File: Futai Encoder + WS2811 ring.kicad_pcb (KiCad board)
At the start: 2 copper layers, 32 x 49 mm, 41 parts, among them J1 Conn_02x05_Top_Bottom, SW1 RotaryEncoder_Switch_RGB

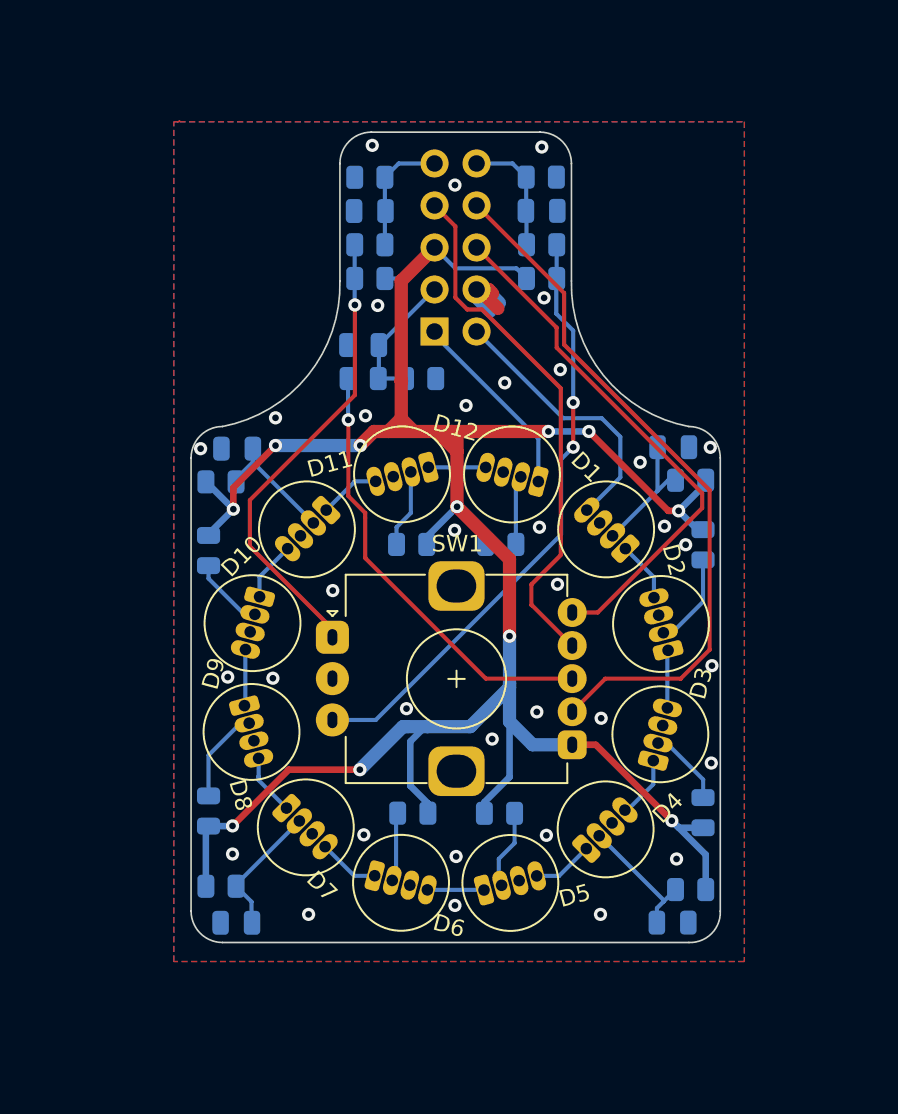
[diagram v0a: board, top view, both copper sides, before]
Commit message: smaller board width, new component placements and better track routing
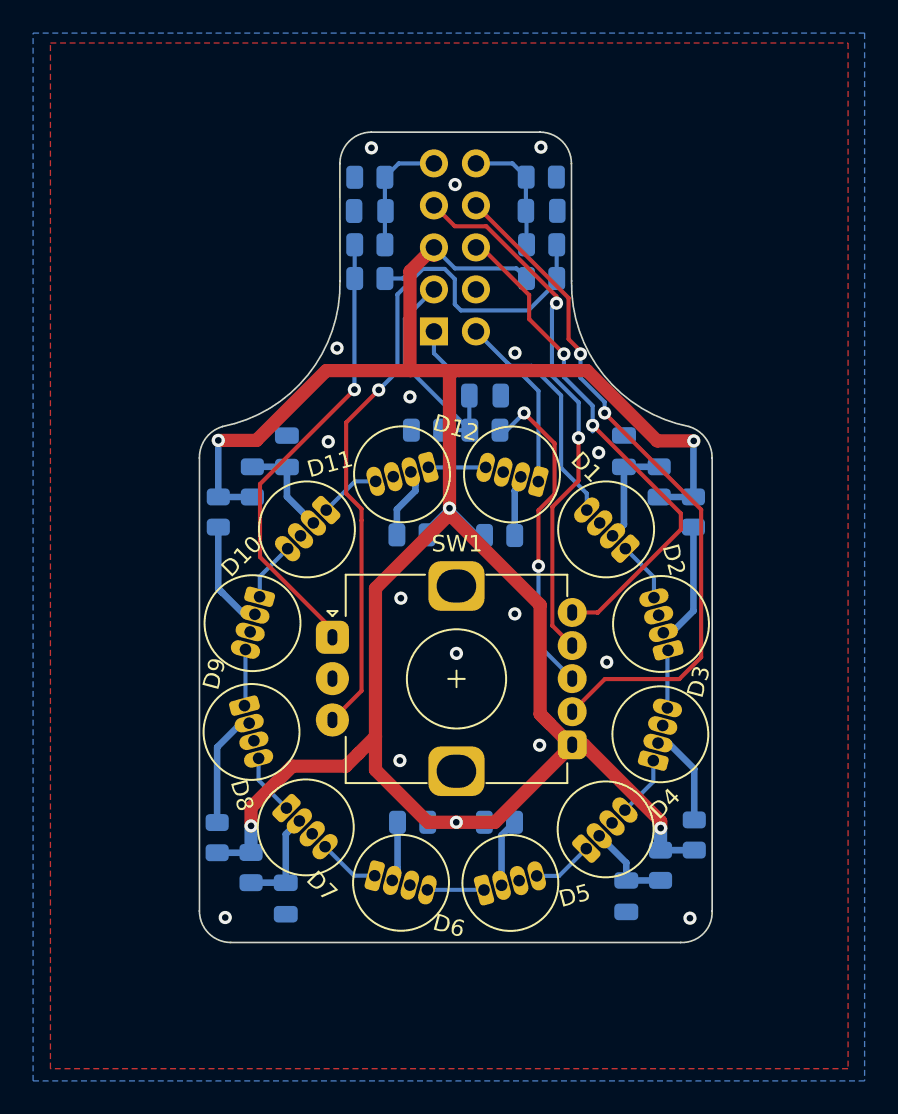
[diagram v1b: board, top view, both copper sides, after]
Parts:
- R1, R10, R11, R12, R2, R3, R4, R5, R6, R7, R8, R9: value 160 -> 130
- moved R21 7.99 mm to (150.3, 84.1), turned to 0 degrees
- moved C21 7.98 mm to (150.3, 82.0), turned to 0 degrees
- moved C7 3.33 mm to (138.2, 112.4), turned to -90 degrees
- moved C4 3.22 mm to (158.8, 112.3), turned to 90 degrees
- moved R22 3.14 mm to (146.7, 84.1), turned to 0 degrees
- moved C10 3.01 mm to (138.3, 85.4), turned to 90 degrees
- moved C1 2.99 mm to (158.7, 85.4), turned to 90 degrees
- moved R9 2.40 mm to (134.1, 89.1)
- moved R4 2.34 mm to (160.9, 110.4), turned to -90 degrees
- moved R7 2.14 mm to (136.1, 110.6), turned to -90 degrees
- moved R2 2.06 mm to (162.9, 89.1)
- moved R1 1.90 mm to (160.8, 87.2), turned to 90 degrees
- moved R10 1.90 mm to (136.2, 87.2), turned to 90 degrees
- moved R8 1.69 mm to (134.1, 108.8)
- moved R3 1.45 mm to (162.9, 108.6)
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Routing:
- net GND: track 10.2 -> 3.29 mm, vias 35 -> 16
- net SWC: track 26.8 -> 20.0 mm, vias 1 -> 2
- net ENC_B: track 36.7 -> 43.4 mm, vias 2 -> 1
- net +5V: track 148.1 -> 154.5 mm, vias 11 -> 6
- net Net-(C21-Pad1): track 8.45 -> 14.7 mm
- net Net-(D9-Pad2): track 4.47 -> 7.63 mm
- net Net-(D2-Pad2): track 6.24 -> 9.17 mm
- net Net-(C4-Pad2): track 8.10 -> 5.49 mm
- net DOUT: track 12.0 -> 14.6 mm
- net Net-(D8-Pad2): track 6.17 -> 8.51 mm
- net Net-(D3-Pad2): track 5.30 -> 7.47 mm
- net DIN: track 16.6 -> 14.6 mm
- net Net-(C7-Pad1): track 8.16 -> 6.27 mm
- net Net-(C10-Pad1): track 7.63 -> 6.16 mm
- net Net-(D12-Pad2): track 4.21 -> 5.47 mm
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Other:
- board size 32 x 49 mm -> 31 x 49 mm
- board text added: "5V"
- board text added: "BLU"
- board text added: "Din"
- board text added: "Dout"
- board text added: "EncB"
- board text added: "GND"
- board text added: "GRE"
- board text added: "RED"
- board text added: "SWC"
- board text added: "https://github.com/andilge"
- board text added: "v0.65"
- board text removed: "A|GR|5|SW|DO"
- board text removed: "B|BL|RE|G|DI"
- board text removed: "https//github.com/andilge"
- board text removed: "v0.5"

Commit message: fixing wrong header pin descrition on borad
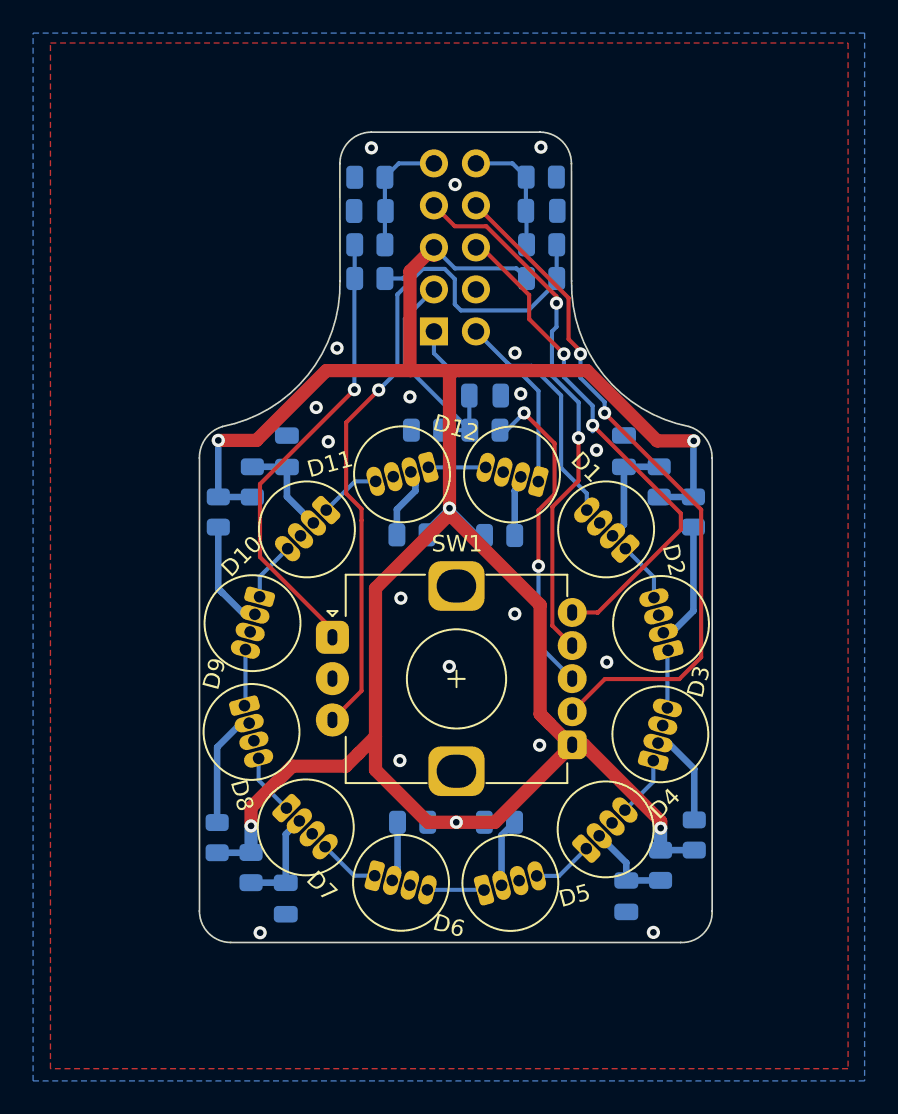
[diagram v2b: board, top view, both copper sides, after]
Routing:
- net GND: vias 16 -> 18
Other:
- board text added: "EncA"
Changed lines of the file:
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@@
     (effects (font (size 0.65 0.65) (thickness 0.1)) (justify mirror))
   )
-  (gr_text "EncB" (at 145.41 68 270) (layer "B.SilkS")
+  (gr_text "EncA" (at 145.41 68 270) (layer "B.SilkS")
     (effects (font (size 0.65 0.65) (thickness 0.1)) (justify mirror))
   )
@@
   (segment (start 145.721259 111.63235) (end 145.721259 112.178741) (width 0.25) (layer "F.Cu") (net 2))
   (segment (start 136.05765 96.321259) (end 135.521259 96.321259) (width 0.25) (layer "F.Cu") (net 2))
-  (via (at 148.54 97.62) (size 0.8) (drill 0.4) (layers "F.Cu" "B.Cu") (free) (net 2))
-  (via (at 157.14 85.48) (size 0.8) (drill 0.4) (layers "F.Cu" "B.Cu") (free) (net 2))
+  (via (at 148.11 98.41) (size 0.8) (drill 0.4) (layers "F.Cu" "B.Cu") (free) (net 2))
+  (via (at 157.01 85.33) (size 0.8) (drill 0.4) (layers "F.Cu" "B.Cu") (free) (net 2))
   (via (at 157.63 98.15) (size 0.8) (drill 0.4) (layers "F.Cu" "B.Cu") (free) (net 2))
   (via (at 143.4 67.05) (size 0.8) (drill 0.4) (layers "F.Cu" "B.Cu") (free) (net 2))
-  (via (at 134.56 113.59) (size 0.8) (drill 0.4) (layers "F.Cu" "B.Cu") (free) (net 2))
+  (via (at 140.06 82.75) (size 0.8) (drill 0.4) (layers "F.Cu" "B.Cu") (free) (net 2))
+  (via (at 136.67 114.51) (size 0.8) (drill 0.4) (layers "F.Cu" "B.Cu") (free) (net 2))
   (via (at 141.32 79.16) (size 0.8) (drill 0.4) (layers "F.Cu" "B.Cu") (free) (net 2))
-  (via (at 162.66 113.63) (size 0.8) (drill 0.4) (layers "F.Cu" "B.Cu") (free) (net 2))
+  (via (at 160.45 114.49) (size 0.8) (drill 0.4) (layers "F.Cu" "B.Cu") (free) (net 2))
   (via (at 140.79 84.82) (size 0.8) (drill 0.4) (layers "F.Cu" "B.Cu") (free) (net 2))
   (via (at 145.12 104.1) (size 0.8) (drill 0.4) (layers "F.Cu" "B.Cu") (free) (net 2))
@@
   (via (at 145.73 82.11) (size 0.8) (drill 0.4) (layers "F.Cu" "B.Cu") (free) (net 2))
   (via (at 152.07 95.23) (size 0.8) (drill 0.4) (layers "F.Cu" "B.Cu") (free) (net 2))
+  (via (at 152.43 81.92) (size 0.8) (drill 0.4) (layers "F.Cu" "B.Cu") (free) (net 2))
   (via (at 153.65 67.01) (size 0.8) (drill 0.4) (layers "F.Cu" "B.Cu") (free) (net 2))
   (segment (start 139.888909 89.731091) (end 139.881091 89.731091) (width 0.25) (layer "B.Cu") (net 3))
@@
   (via (at 155.92 84.59) (size 0.8) (drill 0.4) (layers "F.Cu" "B.Cu") (net 31))
   (via (at 154.59 76.44) (size 0.8) (drill 0.4) (layers "F.Cu" "B.Cu") (net 31))
-  (segment (start 154.315489 76.714511) (end 154.59 76.44) (width 0.25) (layer "B.Cu") (net 31))
-  (segment (start 154.315489 80.829771) (end 154.315489 76.714511) (width 0.25) (layer "B.Cu") (net 31))
-  (segment (start 155.92 84.59) (end 155.93 84.58) (width 0.25) (layer "B.Cu") (net 31))
-  (segment (start 155.93 84.58) (end 155.93 82.444282) (width 0.25) (layer "B.Cu") (net 31))
-  (segment (start 155.93 82.444282) (end 154.315489 80.829771) (width 0.25) (layer "B.Cu") (net 31))
+  (segment (start 155.93 84.58) (end 155.92 84.59) (width 0.25) (layer "B.Cu") (net 31))
+  (segment (start 154.59 76.44) (end 154.59 77.88) (width 0.25) (layer "B.Cu") (net 31))
+  (segment (start 154.315489 78.154511) (end 154.315489 80.829771) (width 0.25) (layer "B.Cu") (net 31))
+  (segment (start 154.59 77.88) (end 154.315489 78.154511) (width 0.25) (layer "B.Cu") (net 31))
+  (segment (start 154.315489 80.829771) (end 155.93 82.444282) (width 0.25) (layer "B.Cu") (net 31))
+  (segment (start 155.93 82.444282) (end 155.93 84.58) (width 0.25) (layer "B.Cu") (net 31))
   (segment (start 154.475522 84.925522) (end 154.475522 87.98876) (width 0.25) (layer "F.Cu") (net 32))
   (segment (start 154.475522 87.98876) (end 153.5 88.964282) (width 0.25) (layer "F.Cu") (net 32))

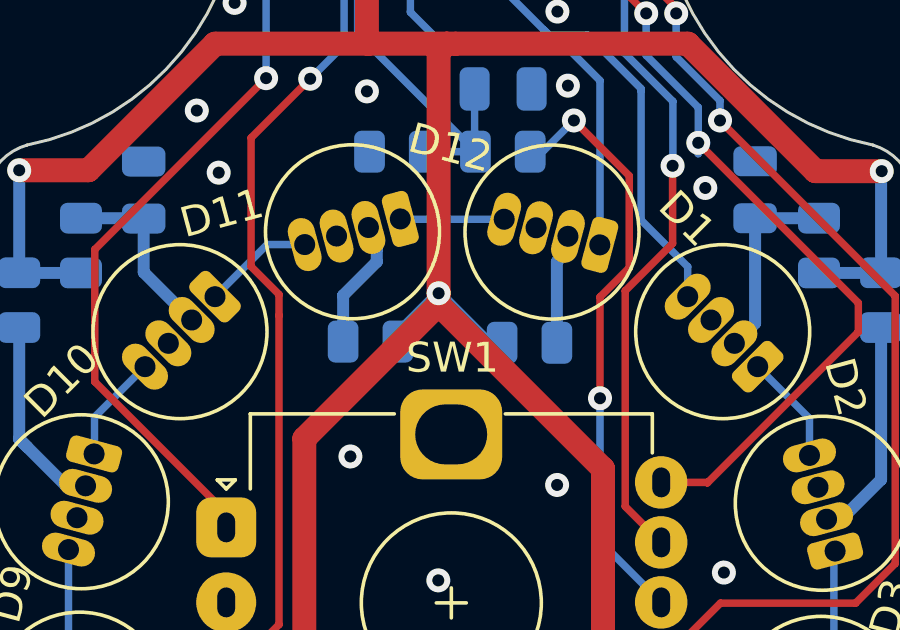
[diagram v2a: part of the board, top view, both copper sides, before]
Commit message: completeing 3d models, adding new images
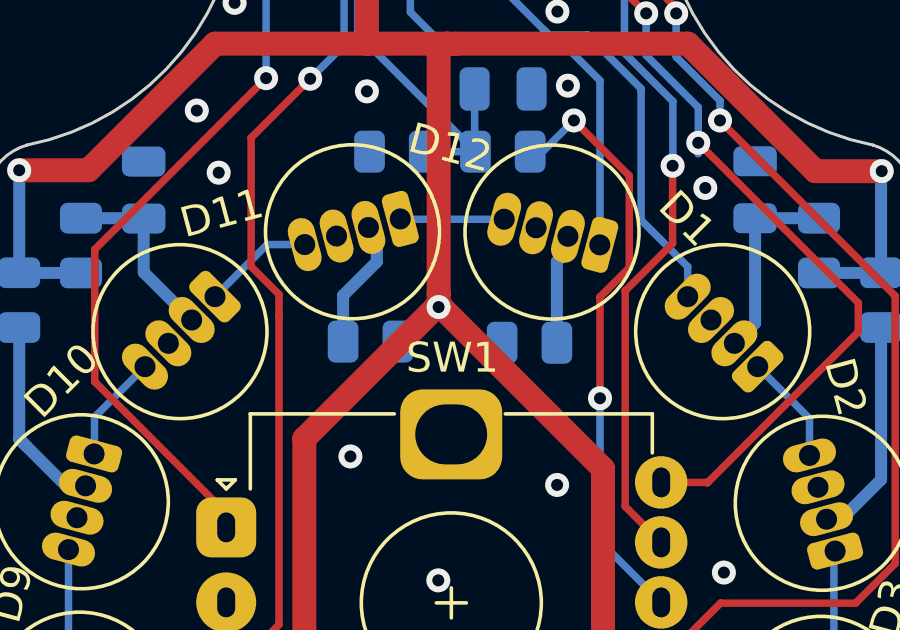
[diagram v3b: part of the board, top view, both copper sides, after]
